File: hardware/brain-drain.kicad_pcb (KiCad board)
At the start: 4 copper layers, 150 x 98 mm, 310 parts, among them J10 SATA 22-pin, J11 SATA 22-pin, J12 SATA 22-pin, J13 SATA 22-pin, J21 KPJX-4S-S, J3 microSD, J4 RJ45 GbE magjack UDE RB1-125B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, J40 Fan GND/5V/TACH/PWM, J41 OLED GND/VCC/SCL/SDA, J5 USB-C rpiboot, J50 M.2 M-key, J6 nRPIBOOT, J7 UART0 GND/TX/RX, M1 CM5002016, Q1 2N7002, Q20 AO4407A, Q31 P-FET -30V 6A DFN3x3, Q32 P-FET -30V 6A DFN3x3, Q33 P-FET -30V 6A DFN3x3, Q34 P-FET -30V 6A DFN3x3, Q41 P-FET -30V 6A DFN3x3, Q42 P-FET -30V 6A DFN3x3, Q43 P-FET -30V 6A DFN3x3, Q44 P-FET -30V 6A DFN3x3, Q51 2N7002, Q52 2N7002, Q53 2N7002, Q54 2N7002, Q61 2N7002, Q62 2N7002, Q63 2N7002, Q64 2N7002, SW1 DIP x8, SW3 door microswitch, U1 USB5744/2G, U10 ASM1153E, U11 ASM1153E, U12 ASM1153E, U13 ASM1153E, U2 USB5744/2G, U20 TPS56637RPAR, U21 TPS56637RPAR, U22 AP63203WU-7, U3 AP2112K-1.2, U50 TPS22965DSGR, U51 AP63203WU-7, U52 TPS22965DSGR, Y1 25MHz CL=20pF, Y10 30MHz CL=16pF, Y11 30MHz CL=16pF, Y12 30MHz CL=16pF, Y13 30MHz CL=16pF, Y2 25MHz CL=20pF

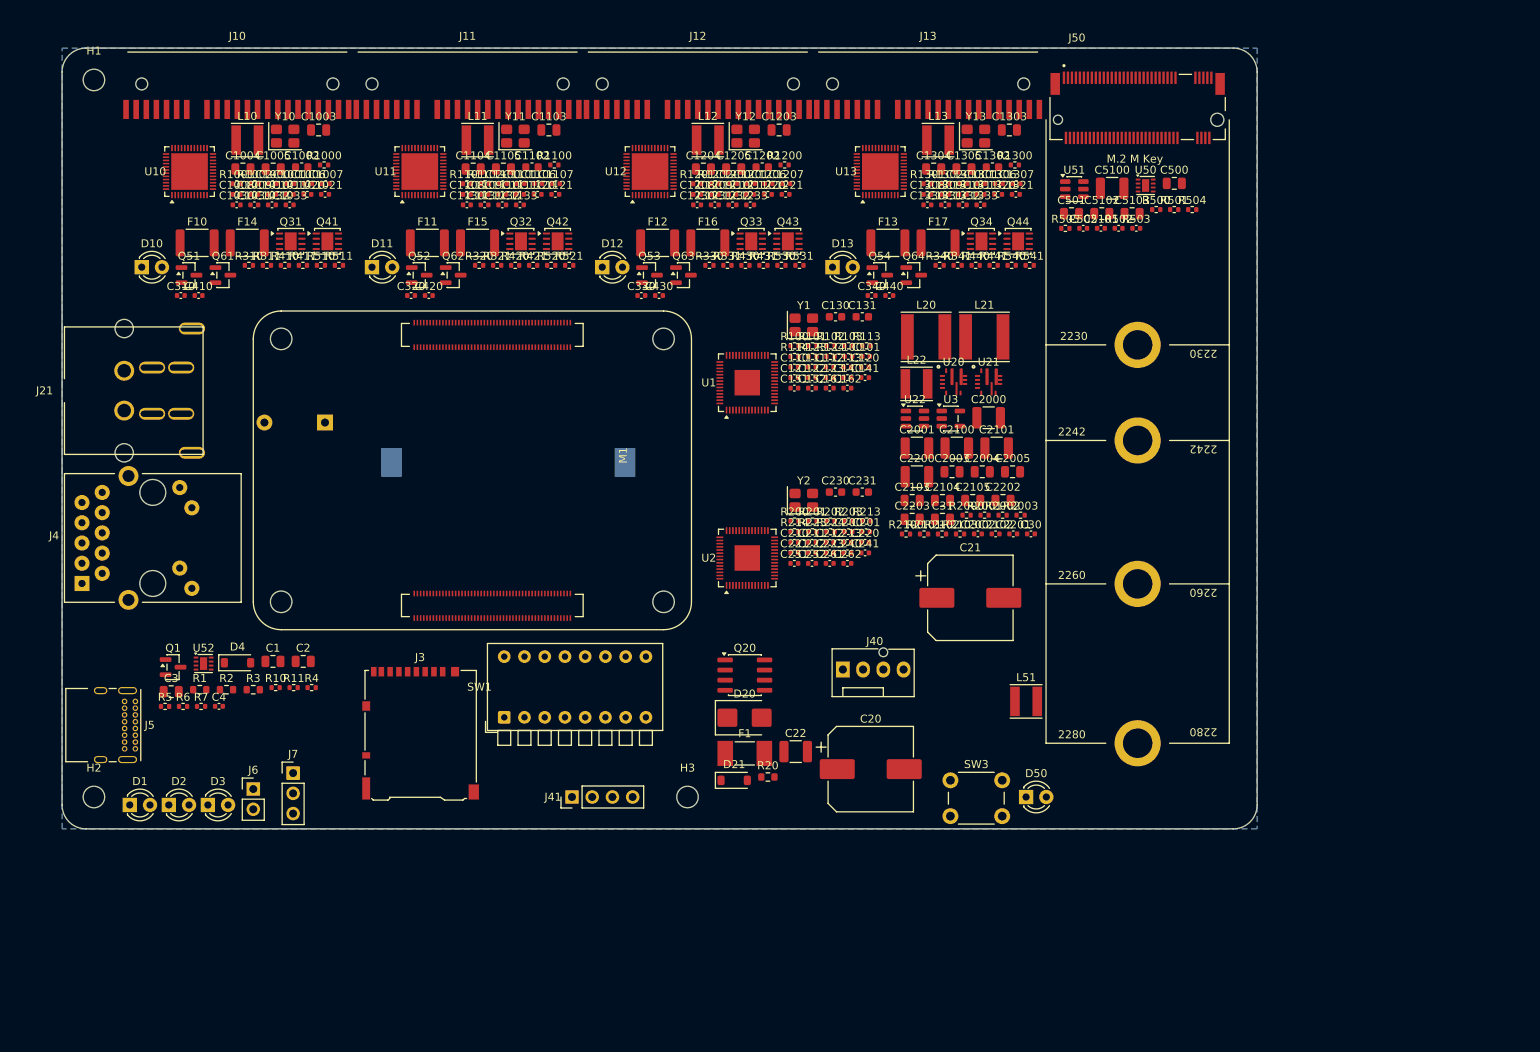
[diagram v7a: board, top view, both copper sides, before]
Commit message: design v2: wireless brain box (C22-C23) — no Ethernet, no buzzer, passive cooler, hinged lid, Wi-Fi AP + QR + phone page, fabrication guide
hardware: 136x100 outline, CM5 wireless antenna edge on the left board edge with a copper-free
strip (rule area), DIN/USB-C/microSD on the right wall, M.2 along the front under the lid, lid
microswitch, CR2032 + service headers on the bottom; magjack and buzzer removed from the
netlist; check_place clean, DRC 0 errors; schematic + connections regenerated, render script
also exports the schematic
software: wifi.py (nmcli / simulated backends, ephemeral key, join, resets), webui.py (stdlib
HTTP phone page: status, certificates, log, join, reset), qr.py, OLED frames with the Wi-Fi QR
code, DIP mode 110 = SERVICE, braindrain wifi-reset; 74 tests, ruff clean; qrcode dependency
enclosure: hinged lid (rear knuckles, filament pin, front snap latch), vents on the antenna side
and front, right-wall cutouts, lid-open scene render
docs: C22/C23, FABRICATION.md (vendors, cost estimate, gates), STATUS R19-R20, panels rear/right,
OLED Wi-Fi mockup, README/ARCHITECTURE/USAGE/BOM/CHANGELOG/HISTORY/tracker updated

Co-Authored-By: Claude Fable 5.1 <noreply@anthropic.com>
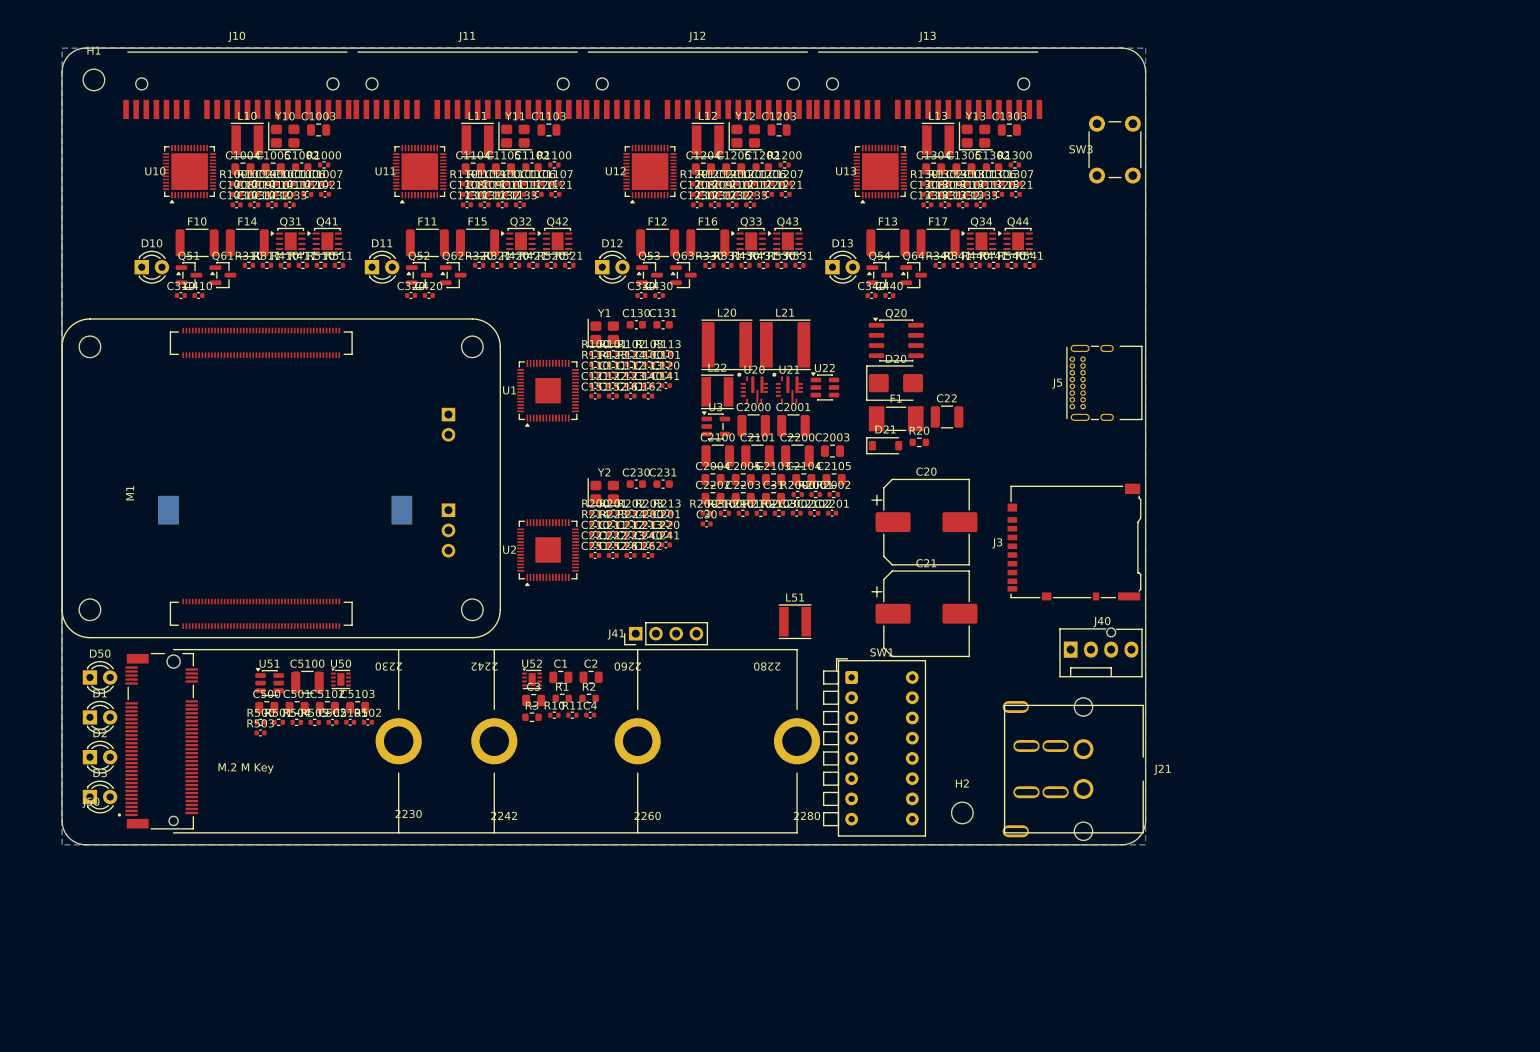
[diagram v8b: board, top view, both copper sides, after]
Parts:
- removed the C340 at (121.6, 51.1)
- removed the C440 at (123.8, 51.1)
- removed the Q64 at (126.9, 48.5)
- removed the R340 at (130.2, 47.3)
- removed the R341 at (132.4, 47.3)
- removed the R440 at (134.7, 47.3)
- removed the R441 at (136.9, 47.3)
- removed the R540 at (139.2, 47.3)
- removed the R541 at (141.4, 47.3)
- BT1: renamed from M1; value CM5002016 -> CR2032; footprint brain-drain:Raspberry-Pi-5-Compute-Module -> Battery:BatteryHolder_Keystone_1060_1x2032; moved to B.Cu
- C1: renamed from R502; value 0R (cap DNP alt) -> 22u 10V; footprint Capacitor_SMD:C_0402_1005Metric -> Capacitor_SMD:C_0805_2012Metric
- C100: renamed from C131; value 4.7u 10V -> 33p; footprint Capacitor_SMD:C_0603_1608Metric -> Capacitor_SMD:C_0402_1005Metric
- C1000: renamed from L10; value 4.7u 1A -> 22p; footprint Inductor_SMD:L_Taiyo-Yuden_NR-40xx -> Capacitor_SMD:C_0402_1005Metric
- C1001: renamed from Y10; value 30MHz CL=16pF -> 22p; footprint Crystal:Crystal_SMD_3225-4Pin_3.2x2.5mm -> Capacitor_SMD:C_0402_1005Metric
- C1002: renamed from C251; value 100n -> 2.2u; footprint Capacitor_SMD:C_0402_1005Metric -> Capacitor_SMD:C_0603_1608Metric
- C1003: renamed from C223; value 100n -> 10u 10V; footprint Capacitor_SMD:C_0402_1005Metric -> Capacitor_SMD:C_0805_2012Metric
- C1004: renamed from C240; value 100n -> 10u 10V; footprint Capacitor_SMD:C_0402_1005Metric -> Capacitor_SMD:C_0805_2012Metric
- C1005: renamed from C241; value 100n -> 10u 10V; footprint Capacitor_SMD:C_0402_1005Metric -> Capacitor_SMD:C_0805_2012Metric
- C1006: renamed from C1003; value 10u 10V -> 100n; footprint Capacitor_SMD:C_0805_2012Metric -> Capacitor_SMD:C_0402_1005Metric
- C1007: renamed from C1004; value 10u 10V -> 100n; footprint Capacitor_SMD:C_0805_2012Metric -> Capacitor_SMD:C_0402_1005Metric
- C1008: renamed from C1005; value 10u 10V -> 100n; footprint Capacitor_SMD:C_0805_2012Metric -> Capacitor_SMD:C_0402_1005Metric
- C1009: renamed from C1002; value 2.2u -> 100n; footprint Capacitor_SMD:C_0603_1608Metric -> Capacitor_SMD:C_0402_1005Metric
- C101: renamed from R100; value 12.0k 1% -> 33p; footprint Resistor_SMD:R_0402_1005Metric -> Capacitor_SMD:C_0402_1005Metric
- C1010: renamed from R1000; value 12.1k 1% -> 100n; footprint Resistor_SMD:R_0402_1005Metric -> Capacitor_SMD:C_0402_1005Metric
- C1011: renamed from R1001; value 10k -> 100n; footprint Resistor_SMD:R_0402_1005Metric -> Capacitor_SMD:C_0402_1005Metric
- C1020: renamed from R1002; value 470 -> 100n; footprint Resistor_SMD:R_0402_1005Metric -> Capacitor_SMD:C_0402_1005Metric
- C1021: renamed from C1000; value 22p -> 100n
- C1030: renamed from C1001; value 22p -> 10n
- C1031: renamed from C1006; value 100n -> 10n
- C1032: renamed from C1007; value 100n -> 10n
- C1033: renamed from C1008; value 100n -> 10n
- C110: renamed from R101; value 10k -> 100n; footprint Resistor_SMD:R_0402_1005Metric -> Capacitor_SMD:C_0402_1005Metric
- C1100: renamed from L11; value 4.7u 1A -> 22p; footprint Inductor_SMD:L_Taiyo-Yuden_NR-40xx -> Capacitor_SMD:C_0402_1005Metric
- C1101: renamed from Y11; value 30MHz CL=16pF -> 22p; footprint Crystal:Crystal_SMD_3225-4Pin_3.2x2.5mm -> Capacitor_SMD:C_0402_1005Metric
- C1102: renamed from R510; value 10k -> 2.2u; footprint Resistor_SMD:R_0402_1005Metric -> Capacitor_SMD:C_0603_1608Metric
- C1103: renamed from R311; value 10k -> 10u 10V; footprint Resistor_SMD:R_0402_1005Metric -> Capacitor_SMD:C_0805_2012Metric
- C1104: renamed from R410; value 100k -> 10u 10V; footprint Resistor_SMD:R_0402_1005Metric -> Capacitor_SMD:C_0805_2012Metric
- C1105: renamed from R411; value 10k -> 10u 10V; footprint Resistor_SMD:R_0402_1005Metric -> Capacitor_SMD:C_0805_2012Metric
- C1106: renamed from C1103; value 10u 10V -> 100n; footprint Capacitor_SMD:C_0805_2012Metric -> Capacitor_SMD:C_0402_1005Metric
- C1107: renamed from C1104; value 10u 10V -> 100n; footprint Capacitor_SMD:C_0805_2012Metric -> Capacitor_SMD:C_0402_1005Metric
- C1108: renamed from C1105; value 10u 10V -> 100n; footprint Capacitor_SMD:C_0805_2012Metric -> Capacitor_SMD:C_0402_1005Metric
- C1109: renamed from C1102; value 2.2u -> 100n; footprint Capacitor_SMD:C_0603_1608Metric -> Capacitor_SMD:C_0402_1005Metric
- C111: renamed from R102; value 10k -> 100n; footprint Resistor_SMD:R_0402_1005Metric -> Capacitor_SMD:C_0402_1005Metric
- C1110: renamed from R1100; value 12.1k 1% -> 100n; footprint Resistor_SMD:R_0402_1005Metric -> Capacitor_SMD:C_0402_1005Metric
- C1111: renamed from R1101; value 10k -> 100n; footprint Resistor_SMD:R_0402_1005Metric -> Capacitor_SMD:C_0402_1005Metric
- C112: renamed from R103; value 200k -> 100n; footprint Resistor_SMD:R_0402_1005Metric -> Capacitor_SMD:C_0402_1005Metric
- C1120: renamed from R1102; value 470 -> 100n; footprint Resistor_SMD:R_0402_1005Metric -> Capacitor_SMD:C_0402_1005Metric
- C1121: renamed from C1100; value 22p -> 100n
- C113: renamed from R113; value 10k -> 100n; footprint Resistor_SMD:R_0402_1005Metric -> Capacitor_SMD:C_0402_1005Metric
- C1130: renamed from C1101; value 22p -> 10n
- C1131: renamed from C1106; value 100n -> 10n
- C1132: renamed from C1107; value 100n -> 10n
- C1133: renamed from C1108; value 100n -> 10n
- C120: renamed from R114; value 10k -> 100n; footprint Resistor_SMD:R_0402_1005Metric -> Capacitor_SMD:C_0402_1005Metric
- C1200: renamed from L12; value 4.7u 1A -> 22p; footprint Inductor_SMD:L_Taiyo-Yuden_NR-40xx -> Capacitor_SMD:C_0402_1005Metric
- C1201: renamed from Y12; value 30MHz CL=16pF -> 22p; footprint Crystal:Crystal_SMD_3225-4Pin_3.2x2.5mm -> Capacitor_SMD:C_0402_1005Metric
- C1202: renamed from R520; value 10k -> 2.2u; footprint Resistor_SMD:R_0402_1005Metric -> Capacitor_SMD:C_0603_1608Metric
- C1203: renamed from R321; value 10k -> 10u 10V; footprint Resistor_SMD:R_0402_1005Metric -> Capacitor_SMD:C_0805_2012Metric
- C1204: renamed from R420; value 100k -> 10u 10V; footprint Resistor_SMD:R_0402_1005Metric -> Capacitor_SMD:C_0805_2012Metric
- C1205: renamed from R421; value 10k -> 10u 10V; footprint Resistor_SMD:R_0402_1005Metric -> Capacitor_SMD:C_0805_2012Metric
- C1206: renamed from C1203; value 10u 10V -> 100n; footprint Capacitor_SMD:C_0805_2012Metric -> Capacitor_SMD:C_0402_1005Metric
- C1207: renamed from C1204; value 10u 10V -> 100n; footprint Capacitor_SMD:C_0805_2012Metric -> Capacitor_SMD:C_0402_1005Metric
- C1208: renamed from C1205; value 10u 10V -> 100n; footprint Capacitor_SMD:C_0805_2012Metric -> Capacitor_SMD:C_0402_1005Metric
- C1209: renamed from C1202; value 2.2u -> 100n; footprint Capacitor_SMD:C_0603_1608Metric -> Capacitor_SMD:C_0402_1005Metric
- C121: renamed from R123; value 10k -> 100n; footprint Resistor_SMD:R_0402_1005Metric -> Capacitor_SMD:C_0402_1005Metric
- C1210: renamed from R1200; value 12.1k 1% -> 100n; footprint Resistor_SMD:R_0402_1005Metric -> Capacitor_SMD:C_0402_1005Metric
- C1211: renamed from R1201; value 10k -> 100n; footprint Resistor_SMD:R_0402_1005Metric -> Capacitor_SMD:C_0402_1005Metric
- C122: renamed from R124; value 10k -> 100n; footprint Resistor_SMD:R_0402_1005Metric -> Capacitor_SMD:C_0402_1005Metric
- C1220: renamed from R1202; value 470 -> 100n; footprint Resistor_SMD:R_0402_1005Metric -> Capacitor_SMD:C_0402_1005Metric
- C1221: renamed from C1200; value 22p -> 100n
- C123: renamed from C100; value 33p -> 100n
- C1230: renamed from C1201; value 22p -> 10n
- C1231: renamed from C1206; value 100n -> 10n
- C1232: renamed from C1207; value 100n -> 10n
- C1233: renamed from C1208; value 100n -> 10n
- C130: renamed from R3; value 1k -> 4.7u 10V; footprint Resistor_SMD:R_0603_1608Metric -> Capacitor_SMD:C_0603_1608Metric
- C1300: renamed from L13; value 4.7u 1A -> 22p; footprint Inductor_SMD:L_Taiyo-Yuden_NR-40xx -> Capacitor_SMD:C_0402_1005Metric
- C1301: renamed from Y13; value 30MHz CL=16pF -> 22p; footprint Crystal:Crystal_SMD_3225-4Pin_3.2x2.5mm -> Capacitor_SMD:C_0402_1005Metric
- C1302: renamed from R530; value 10k -> 2.2u; footprint Resistor_SMD:R_0402_1005Metric -> Capacitor_SMD:C_0603_1608Metric
- C1303: renamed from R331; value 10k -> 10u 10V; footprint Resistor_SMD:R_0402_1005Metric -> Capacitor_SMD:C_0805_2012Metric
- C1304: renamed from R430; value 100k -> 10u 10V; footprint Resistor_SMD:R_0402_1005Metric -> Capacitor_SMD:C_0805_2012Metric
- C1305: renamed from R431; value 10k -> 10u 10V; footprint Resistor_SMD:R_0402_1005Metric -> Capacitor_SMD:C_0805_2012Metric
- C1306: renamed from C1303; value 10u 10V -> 100n; footprint Capacitor_SMD:C_0805_2012Metric -> Capacitor_SMD:C_0402_1005Metric
- C1307: renamed from C1304; value 10u 10V -> 100n; footprint Capacitor_SMD:C_0805_2012Metric -> Capacitor_SMD:C_0402_1005Metric
- C1308: renamed from C1305; value 10u 10V -> 100n; footprint Capacitor_SMD:C_0805_2012Metric -> Capacitor_SMD:C_0402_1005Metric
- C1309: renamed from C1302; value 2.2u -> 100n; footprint Capacitor_SMD:C_0603_1608Metric -> Capacitor_SMD:C_0402_1005Metric
- C131: renamed from R10; value 10k -> 4.7u 10V; footprint Resistor_SMD:R_0402_1005Metric -> Capacitor_SMD:C_0603_1608Metric
- C1310: renamed from R1300; value 12.1k 1% -> 100n; footprint Resistor_SMD:R_0402_1005Metric -> Capacitor_SMD:C_0402_1005Metric
- C1311: renamed from R1301; value 10k -> 100n; footprint Resistor_SMD:R_0402_1005Metric -> Capacitor_SMD:C_0402_1005Metric
- C1320: renamed from R1302; value 470 -> 100n; footprint Resistor_SMD:R_0402_1005Metric -> Capacitor_SMD:C_0402_1005Metric
- C1321: renamed from C1300; value 22p -> 100n
- C1330: renamed from C1301; value 22p -> 10n
- C1331: renamed from C1306; value 100n -> 10n
- C1332: renamed from C1307; value 100n -> 10n
- C1333: renamed from C1308; value 100n -> 10n
- C140: renamed from C101; value 33p -> 100n
- C2: renamed from R503; value 0R (cap DNP alt) -> 22u 10V; footprint Capacitor_SMD:C_0402_1005Metric -> Capacitor_SMD:C_0805_2012Metric
- C20: renamed from J21; value KPJX-4S-S -> 680u 25V low-ESR; footprint brain-drain:Kycon_KPJX-4S-S -> Capacitor_SMD:CP_Elec_10x10.5
- C200: renamed from C231; value 4.7u 10V -> 33p; footprint Capacitor_SMD:C_0603_1608Metric -> Capacitor_SMD:C_0402_1005Metric
- C2000: renamed from U21; value TPS56637RPAR -> 10u 25V; footprint brain-drain:Texas_RPA0010A_VQFN-HR-10_3x3mm -> Capacitor_SMD:C_1210_3225Metric
- C2001: renamed from U22; value AP63203WU-7 -> 10u 25V; footprint Package_TO_SOT_SMD:TSOT-23-6 -> Capacitor_SMD:C_1210_3225Metric
- C2002: renamed from R2101; value 10k -> 100n 25V; footprint Resistor_SMD:R_0402_1005Metric -> Capacitor_SMD:C_0402_1005Metric
- C2003: renamed from C2100; value 10u 25V -> 22u 10V; footprint Capacitor_SMD:C_1210_3225Metric -> Capacitor_SMD:C_0805_2012Metric
- C2004: renamed from C2101; value 10u 25V -> 22u 10V; footprint Capacitor_SMD:C_1210_3225Metric -> Capacitor_SMD:C_0805_2012Metric
- C2005: renamed from C2200; value 10u 25V -> 22u 10V; footprint Capacitor_SMD:C_1210_3225Metric -> Capacitor_SMD:C_0805_2012Metric
- C201: renamed from R200; value 12.0k 1% -> 33p; footprint Resistor_SMD:R_0402_1005Metric -> Capacitor_SMD:C_0402_1005Metric
- C210: renamed from R201; value 10k -> 100n; footprint Resistor_SMD:R_0402_1005Metric -> Capacitor_SMD:C_0402_1005Metric
- C2100: renamed from U3; value AP2112K-1.2 -> 10u 25V; footprint Package_TO_SOT_SMD:SOT-23-5 -> Capacitor_SMD:C_1210_3225Metric
- C2102: renamed from R2102; value 100k -> 100n 25V; footprint Resistor_SMD:R_0402_1005Metric -> Capacitor_SMD:C_0402_1005Metric
- C211: renamed from R202; value 10k -> 100n; footprint Resistor_SMD:R_0402_1005Metric -> Capacitor_SMD:C_0402_1005Metric
- C212: renamed from R203; value 200k -> 100n; footprint Resistor_SMD:R_0402_1005Metric -> Capacitor_SMD:C_0402_1005Metric
- C213: renamed from R213; value 10k -> 100n; footprint Resistor_SMD:R_0402_1005Metric -> Capacitor_SMD:C_0402_1005Metric
- C22: renamed from Q20; value AO4407A -> 10u 25V; footprint Package_SO:SOIC-8_3.9x4.9mm_P1.27mm -> Capacitor_SMD:C_1210_3225Metric
- C220: renamed from R214; value 10k -> 100n; footprint Resistor_SMD:R_0402_1005Metric -> Capacitor_SMD:C_0402_1005Metric
- C2201: renamed from R2103; value 10k -> 100n 10V; footprint Resistor_SMD:R_0402_1005Metric -> Capacitor_SMD:C_0402_1005Metric
- C221: renamed from R223; value 10k -> 100n; footprint Resistor_SMD:R_0402_1005Metric -> Capacitor_SMD:C_0402_1005Metric
- C222: renamed from R224; value 10k -> 100n; footprint Resistor_SMD:R_0402_1005Metric -> Capacitor_SMD:C_0402_1005Metric
- C223: renamed from C200; value 33p -> 100n
- C230: renamed from C122; value 100n -> 4.7u 10V; footprint Capacitor_SMD:C_0402_1005Metric -> Capacitor_SMD:C_0603_1608Metric
- C231: renamed from C123; value 100n -> 4.7u 10V; footprint Capacitor_SMD:C_0402_1005Metric -> Capacitor_SMD:C_0603_1608Metric
- C240: renamed from C201; value 33p -> 100n
- C3: renamed from Q1; value 2N7002 -> 10u 10V; footprint Package_TO_SOT_SMD:SOT-23 -> Capacitor_SMD:C_0805_2012Metric
- C30: renamed from C2002; value 100n 25V -> 1u 10V
- C31: renamed from C2105; value 22u 10V -> 10u 10V
- C310: renamed from Q41; value P-FET -30V 6A DFN3x3 -> 100n; footprint Package_DFN_QFN:DFN-8-1EP_3x3mm_P0.65mm_EP1.5x2.25mm -> Capacitor_SMD:C_0402_1005Metric
- C320: renamed from Q42; value P-FET -30V 6A DFN3x3 -> 100n; footprint Package_DFN_QFN:DFN-8-1EP_3x3mm_P0.65mm_EP1.5x2.25mm -> Capacitor_SMD:C_0402_1005Metric
- C330: renamed from Q43; value P-FET -30V 6A DFN3x3 -> 100n; footprint Package_DFN_QFN:DFN-8-1EP_3x3mm_P0.65mm_EP1.5x2.25mm -> Capacitor_SMD:C_0402_1005Metric
- C340: renamed from Q44; value P-FET -30V 6A DFN3x3 -> 100n; footprint Package_DFN_QFN:DFN-8-1EP_3x3mm_P0.65mm_EP1.5x2.25mm -> Capacitor_SMD:C_0402_1005Metric
- C4: renamed from R1; value 1k -> 1u 10V; footprint Resistor_SMD:R_0603_1608Metric -> Capacitor_SMD:C_0402_1005Metric
- C410: renamed from Q51; value 2N7002 -> 100n; footprint Package_TO_SOT_SMD:SOT-23 -> Capacitor_SMD:C_0402_1005Metric
- C420: renamed from Q52; value 2N7002 -> 100n; footprint Package_TO_SOT_SMD:SOT-23 -> Capacitor_SMD:C_0402_1005Metric
- C430: renamed from Q53; value 2N7002 -> 100n; footprint Package_TO_SOT_SMD:SOT-23 -> Capacitor_SMD:C_0402_1005Metric
- C440: renamed from Q54; value 2N7002 -> 100n; footprint Package_TO_SOT_SMD:SOT-23 -> Capacitor_SMD:C_0402_1005Metric
- C500: renamed from U51; value AP63203WU-7 -> 10u 10V; footprint Package_TO_SOT_SMD:TSOT-23-6 -> Capacitor_SMD:C_0805_2012Metric
- C501: renamed from C5100; value 10u 25V -> 22u 10V; footprint Capacitor_SMD:C_1210_3225Metric -> Capacitor_SMD:C_0805_2012Metric
- C502: renamed from R501; value 10k -> 1n; footprint Resistor_SMD:R_0402_1005Metric -> Capacitor_SMD:C_0402_1005Metric
- C5100: renamed from C2201; value 100n 10V -> 10u 25V; footprint Capacitor_SMD:C_0402_1005Metric -> Capacitor_SMD:C_1210_3225Metric
- C5101: renamed from R504; value 10k -> 100n 10V; footprint Resistor_SMD:R_0402_1005Metric -> Capacitor_SMD:C_0402_1005Metric
- C5102: renamed from U50; value TPS22965DSGR -> 22u 10V; footprint Package_SON:Texas_DSG0008A_WSON-8-1EP_2x2mm_P0.5mm_EP0.9x1.6mm -> Capacitor_SMD:C_0805_2012Metric
- C5103: renamed from C500; value 10u 10V -> 22u 10V
- D1: renamed from J40; value Fan GND/5V/TACH/PWM -> green PWR; footprint Connector:FanPinHeader_1x04_P2.54mm_Vertical -> LED_THT:LED_D3.0mm
- D10: renamed from U2; value USB5744/2G -> blue bay activity; footprint Package_DFN_QFN:QFN-56-1EP_7x7mm_P0.4mm_EP3.2x3.2mm -> LED_THT:LED_D3.0mm
- D2: renamed from D1; value green PWR -> green ACT
- D20: renamed from D50; value blue M.2 activity -> SMBJ15A; footprint LED_THT:LED_D3.0mm -> Diode_SMD:D_SMB
- D21: renamed from D20; value SMBJ15A -> 12V 0.5W; footprint Diode_SMD:D_SMB -> Diode_SMD:D_SOD-123
- D3: renamed from D2; value green ACT -> red STATUS
- D50: renamed from J13; value SATA 22-pin -> blue M.2 activity; footprint brain-drain:SATA_22pin_Receptacle_RA -> LED_THT:LED_D3.0mm
- F1: renamed from SW3; value door microswitch -> 10A slow 0453010.MR; footprint Button_Switch_THT:SW_PUSH_6mm -> Fuse:Fuse_Littelfuse-NANO2-451_453
- F10: renamed from C1009; value 100n -> 3A hold 1812; footprint Capacitor_SMD:C_0402_1005Metric -> Fuse:Fuse_1812_4532Metric
- F11: renamed from C1109; value 100n -> 3A hold 1812; footprint Capacitor_SMD:C_0402_1005Metric -> Fuse:Fuse_1812_4532Metric
- F12: renamed from C1209; value 100n -> 3A hold 1812; footprint Capacitor_SMD:C_0402_1005Metric -> Fuse:Fuse_1812_4532Metric
- F13: renamed from C1309; value 100n -> 3A hold 1812; footprint Capacitor_SMD:C_0402_1005Metric -> Fuse:Fuse_1812_4532Metric
- F14: renamed from C1010; value 100n -> 2A hold 1812; footprint Capacitor_SMD:C_0402_1005Metric -> Fuse:Fuse_1812_4532Metric
- F15: renamed from C1110; value 100n -> 2A hold 1812; footprint Capacitor_SMD:C_0402_1005Metric -> Fuse:Fuse_1812_4532Metric
- F16: renamed from C1210; value 100n -> 2A hold 1812; footprint Capacitor_SMD:C_0402_1005Metric -> Fuse:Fuse_1812_4532Metric
- F17: renamed from C1310; value 100n -> 2A hold 1812; footprint Capacitor_SMD:C_0402_1005Metric -> Fuse:Fuse_1812_4532Metric
- J10: renamed from U1; value USB5744/2G -> SATA 22-pin; footprint Package_DFN_QFN:QFN-56-1EP_7x7mm_P0.4mm_EP3.2x3.2mm -> brain-drain:SATA_22pin_Receptacle_RA
- J21: renamed from H3; value M2.5 -> KPJX-4S-S; footprint MountingHole:MountingHole_2.7mm_M2.5 -> brain-drain:Kycon_KPJX-4S-S
- J3: renamed from BZ1; value 5V magnetic -> microSD; footprint Buzzer_Beeper:Buzzer_12x9.5RM7.6 -> Connector_Card:microSD_HC_Hirose_DM3AT-SF-PEJM5; moved to F.Cu
- J40: renamed from J7; value UART0 GND/TX/RX -> Fan GND/5V/TACH/PWM; footprint Connector_PinHeader_2.54mm:PinHeader_1x03_P2.54mm_Vertical -> Connector:FanPinHeader_1x04_P2.54mm_Vertical
- J41: renamed from SW1; value DIP x8 -> OLED GND/VCC/SCL/SDA; footprint Button_Switch_THT:SW_DIP_SPSTx08_Piano_10.8x21.88mm_W7.62mm_P2.54mm -> Connector_PinHeader_2.54mm:PinHeader_1x04_P2.54mm_Vertical
- J5: renamed from J41; value OLED GND/VCC/SCL/SDA -> USB-C rpiboot; footprint Connector_PinHeader_2.54mm:PinHeader_1x04_P2.54mm_Vertical -> Connector_USB:USB_C_Receptacle_GCT_USB4085
- J50: renamed from U13; value ASM1153E -> M.2 M-key; footprint Package_DFN_QFN:QFN-48-1EP_6x6mm_P0.4mm_EP4.6x4.6mm -> brain-drain:M2_Socket3_MKey_CM5IO
- J6: renamed from BT1; value CR2032 -> nRPIBOOT; footprint Battery:BatteryHolder_Keystone_1060_1x2032 -> Connector_PinHeader_2.54mm:PinHeader_1x02_P2.54mm_Vertical
- J7: renamed from J6; value nRPIBOOT -> UART0 GND/TX/RX; footprint Connector_PinHeader_2.54mm:PinHeader_1x02_P2.54mm_Vertical -> Connector_PinHeader_2.54mm:PinHeader_1x03_P2.54mm_Vertical; moved to B.Cu
- L10: renamed from C221; value 100n -> 4.7u 1A; footprint Capacitor_SMD:C_0402_1005Metric -> Inductor_SMD:L_Taiyo-Yuden_NR-40xx
- L11: renamed from Q61; value 2N7002 -> 4.7u 1A; footprint Package_TO_SOT_SMD:SOT-23 -> Inductor_SMD:L_Taiyo-Yuden_NR-40xx
- L12: renamed from Q62; value 2N7002 -> 4.7u 1A; footprint Package_TO_SOT_SMD:SOT-23 -> Inductor_SMD:L_Taiyo-Yuden_NR-40xx
- L13: renamed from Q63; value 2N7002 -> 4.7u 1A; footprint Package_TO_SOT_SMD:SOT-23 -> Inductor_SMD:L_Taiyo-Yuden_NR-40xx
- L20: renamed from C22; value 10u 25V -> 2.2u 8A; footprint Capacitor_SMD:C_1210_3225Metric -> Inductor_SMD:L_Taiyo-Yuden_NR-60xx
- L21: renamed from D21; value 12V 0.5W -> 2.2u 8A; footprint Diode_SMD:D_SOD-123 -> Inductor_SMD:L_Taiyo-Yuden_NR-60xx
- L22: renamed from R20; value 100k -> 4.7u 3A; footprint Resistor_SMD:R_0603_1608Metric -> Inductor_SMD:L_Taiyo-Yuden_NR-40xx
- L51: renamed from C21; value 680u 25V low-ESR -> 4.7u 3A; footprint Capacitor_SMD:CP_Elec_10x10.5 -> Inductor_SMD:L_Taiyo-Yuden_NR-40xx
- M1: renamed from L51; value 4.7u 3A -> CM5002016; footprint Inductor_SMD:L_Taiyo-Yuden_NR-40xx -> brain-drain:Raspberry-Pi-5-Compute-Module
- Q20: renamed from J50; value M.2 M-key -> AO4407A; footprint brain-drain:M2_Socket3_MKey_CM5IO -> Package_SO:SOIC-8_3.9x4.9mm_P1.27mm
- Q31: renamed from C1011; value 100n -> P-FET -30V 6A DFN3x3; footprint Capacitor_SMD:C_0402_1005Metric -> Package_DFN_QFN:DFN-8-1EP_3x3mm_P0.65mm_EP1.5x2.25mm
- Q32: renamed from C1111; value 100n -> P-FET -30V 6A DFN3x3; footprint Capacitor_SMD:C_0402_1005Metric -> Package_DFN_QFN:DFN-8-1EP_3x3mm_P0.65mm_EP1.5x2.25mm
- Q33: renamed from C1211; value 100n -> P-FET -30V 6A DFN3x3; footprint Capacitor_SMD:C_0402_1005Metric -> Package_DFN_QFN:DFN-8-1EP_3x3mm_P0.65mm_EP1.5x2.25mm
- Q34: renamed from C1311; value 100n -> P-FET -30V 6A DFN3x3; footprint Capacitor_SMD:C_0402_1005Metric -> Package_DFN_QFN:DFN-8-1EP_3x3mm_P0.65mm_EP1.5x2.25mm
- Q41: renamed from C1020; value 100n -> P-FET -30V 6A DFN3x3; footprint Capacitor_SMD:C_0402_1005Metric -> Package_DFN_QFN:DFN-8-1EP_3x3mm_P0.65mm_EP1.5x2.25mm
- Q42: renamed from C1120; value 100n -> P-FET -30V 6A DFN3x3; footprint Capacitor_SMD:C_0402_1005Metric -> Package_DFN_QFN:DFN-8-1EP_3x3mm_P0.65mm_EP1.5x2.25mm
- Q43: renamed from C1220; value 100n -> P-FET -30V 6A DFN3x3; footprint Capacitor_SMD:C_0402_1005Metric -> Package_DFN_QFN:DFN-8-1EP_3x3mm_P0.65mm_EP1.5x2.25mm
- Q44: renamed from C1320; value 100n -> P-FET -30V 6A DFN3x3; footprint Capacitor_SMD:C_0402_1005Metric -> Package_DFN_QFN:DFN-8-1EP_3x3mm_P0.65mm_EP1.5x2.25mm
- Q51: renamed from C1021; value 100n -> 2N7002; footprint Capacitor_SMD:C_0402_1005Metric -> Package_TO_SOT_SMD:SOT-23
- Q52: renamed from C1121; value 100n -> 2N7002; footprint Capacitor_SMD:C_0402_1005Metric -> Package_TO_SOT_SMD:SOT-23
- Q53: renamed from C1221; value 100n -> 2N7002; footprint Capacitor_SMD:C_0402_1005Metric -> Package_TO_SOT_SMD:SOT-23
- Q54: renamed from C1321; value 100n -> 2N7002; footprint Capacitor_SMD:C_0402_1005Metric -> Package_TO_SOT_SMD:SOT-23
- Q61: renamed from C1030; value 10n -> 2N7002; footprint Capacitor_SMD:C_0402_1005Metric -> Package_TO_SOT_SMD:SOT-23
- Q62: renamed from C1130; value 10n -> 2N7002; footprint Capacitor_SMD:C_0402_1005Metric -> Package_TO_SOT_SMD:SOT-23
- Q63: renamed from C1230; value 10n -> 2N7002; footprint Capacitor_SMD:C_0402_1005Metric -> Package_TO_SOT_SMD:SOT-23
- Q64: renamed from C1330; value 10n -> 2N7002; footprint Capacitor_SMD:C_0402_1005Metric -> Package_TO_SOT_SMD:SOT-23
- R1: renamed from U52; value TPS22965DSGR -> 1k; footprint Package_SON:Texas_DSG0008A_WSON-8-1EP_2x2mm_P0.5mm_EP0.9x1.6mm -> Resistor_SMD:R_0603_1608Metric
- R10: renamed from C2; value 22u 10V -> 10k; footprint Capacitor_SMD:C_0805_2012Metric -> Resistor_SMD:R_0402_1005Metric
- R100: renamed from R11; value 10k -> 12.0k 1%
- R1000: renamed from C252; value 100n -> 12.1k 1%; footprint Capacitor_SMD:C_0402_1005Metric -> Resistor_SMD:R_0402_1005Metric
- R1001: renamed from C261; value 100n -> 10k; footprint Capacitor_SMD:C_0402_1005Metric -> Resistor_SMD:R_0402_1005Metric
- R1002: renamed from C262; value 100n -> 470; footprint Capacitor_SMD:C_0402_1005Metric -> Resistor_SMD:R_0402_1005Metric
- R101: renamed from R4; value 1k -> 10k
- R102: renamed from R5; value 100k -> 10k
- R103: renamed from R6; value 470 -> 200k
- R11: renamed from C3; value 10u 10V -> 10k; footprint Capacitor_SMD:C_0805_2012Metric -> Resistor_SMD:R_0402_1005Metric
- R1100: renamed from R511; value 1k -> 12.1k 1%
- R1101: renamed from C310; value 100n -> 10k; footprint Capacitor_SMD:C_0402_1005Metric -> Resistor_SMD:R_0402_1005Metric
- R1102: renamed from C410; value 100n -> 470; footprint Capacitor_SMD:C_0402_1005Metric -> Resistor_SMD:R_0402_1005Metric
- R113: renamed from R7; value 470 -> 10k
- R114: renamed from C4; value 1u 10V -> 10k; footprint Capacitor_SMD:C_0402_1005Metric -> Resistor_SMD:R_0402_1005Metric
- R1200: renamed from R521; value 1k -> 12.1k 1%
- R1201: renamed from C320; value 100n -> 10k; footprint Capacitor_SMD:C_0402_1005Metric -> Resistor_SMD:R_0402_1005Metric
- R1202: renamed from C420; value 100n -> 470; footprint Capacitor_SMD:C_0402_1005Metric -> Resistor_SMD:R_0402_1005Metric
- R123: renamed from Y1; value 25MHz CL=20pF -> 10k; footprint Crystal:Crystal_SMD_3225-4Pin_3.2x2.5mm -> Resistor_SMD:R_0402_1005Metric
- R124: renamed from C130; value 4.7u 10V -> 10k; footprint Capacitor_SMD:C_0603_1608Metric -> Resistor_SMD:R_0402_1005Metric
- R1300: renamed from R531; value 1k -> 12.1k 1%
- R1301: renamed from C330; value 100n -> 10k; footprint Capacitor_SMD:C_0402_1005Metric -> Resistor_SMD:R_0402_1005Metric
- R1302: renamed from C430; value 100n -> 470; footprint Capacitor_SMD:C_0402_1005Metric -> Resistor_SMD:R_0402_1005Metric
- R2: renamed from D4; value 1N4148W -> 1k; footprint Diode_SMD:D_SOD-123 -> Resistor_SMD:R_0603_1608Metric
- R20: renamed from F1; value 10A slow 0453010.MR -> 100k; footprint Fuse:Fuse_Littelfuse-NANO2-451_453 -> Resistor_SMD:R_0603_1608Metric
- R200: renamed from C140; value 100n -> 12.0k 1%; footprint Capacitor_SMD:C_0402_1005Metric -> Resistor_SMD:R_0402_1005Metric
- R2000: renamed from C2202; value 22u 10V -> 73.2k; footprint Capacitor_SMD:C_0805_2012Metric -> Resistor_SMD:R_0402_1005Metric
- R2001: renamed from C2203; value 22u 10V -> 10k; footprint Capacitor_SMD:C_0805_2012Metric -> Resistor_SMD:R_0402_1005Metric
- R2002: renamed from C31; value 10u 10V -> 100k; footprint Capacitor_SMD:C_0805_2012Metric -> Resistor_SMD:R_0402_1005Metric
- R2003: renamed from R2000; value 73.2k -> 10k
- R201: renamed from C141; value 100n -> 10k; footprint Capacitor_SMD:C_0402_1005Metric -> Resistor_SMD:R_0402_1005Metric
- R202: renamed from C151; value 100n -> 10k; footprint Capacitor_SMD:C_0402_1005Metric -> Resistor_SMD:R_0402_1005Metric
- R203: renamed from C152; value 100n -> 200k; footprint Capacitor_SMD:C_0402_1005Metric -> Resistor_SMD:R_0402_1005Metric
- R2100: renamed from R2001; value 10k -> 73.2k
- R2101: renamed from R2002; value 100k -> 10k
- R2102: renamed from R2003; value 10k -> 100k
- R2103: renamed from R2100; value 73.2k -> 10k
- R213: renamed from C161; value 100n -> 10k; footprint Capacitor_SMD:C_0402_1005Metric -> Resistor_SMD:R_0402_1005Metric
- R214: renamed from C162; value 100n -> 10k; footprint Capacitor_SMD:C_0402_1005Metric -> Resistor_SMD:R_0402_1005Metric
- R223: renamed from Y2; value 25MHz CL=20pF -> 10k; footprint Crystal:Crystal_SMD_3225-4Pin_3.2x2.5mm -> Resistor_SMD:R_0402_1005Metric
- R224: renamed from C230; value 4.7u 10V -> 10k; footprint Capacitor_SMD:C_0603_1608Metric -> Resistor_SMD:R_0402_1005Metric
- R3: renamed from C1; value 22u 10V -> 1k; footprint Capacitor_SMD:C_0805_2012Metric -> Resistor_SMD:R_0603_1608Metric
- R310: renamed from C1031; value 10n -> 100k; footprint Capacitor_SMD:C_0402_1005Metric -> Resistor_SMD:R_0402_1005Metric
- R311: renamed from C1032; value 10n -> 10k; footprint Capacitor_SMD:C_0402_1005Metric -> Resistor_SMD:R_0402_1005Metric
- R320: renamed from C1131; value 10n -> 100k; footprint Capacitor_SMD:C_0402_1005Metric -> Resistor_SMD:R_0402_1005Metric
- R321: renamed from C1132; value 10n -> 10k; footprint Capacitor_SMD:C_0402_1005Metric -> Resistor_SMD:R_0402_1005Metric
- R330: renamed from C1231; value 10n -> 100k; footprint Capacitor_SMD:C_0402_1005Metric -> Resistor_SMD:R_0402_1005Metric
- R331: renamed from C1232; value 10n -> 10k; footprint Capacitor_SMD:C_0402_1005Metric -> Resistor_SMD:R_0402_1005Metric
- R340: renamed from C1331; value 10n -> 100k; footprint Capacitor_SMD:C_0402_1005Metric -> Resistor_SMD:R_0402_1005Metric
- R341: renamed from C1332; value 10n -> 10k; footprint Capacitor_SMD:C_0402_1005Metric -> Resistor_SMD:R_0402_1005Metric
- R410: renamed from C1033; value 10n -> 100k; footprint Capacitor_SMD:C_0402_1005Metric -> Resistor_SMD:R_0402_1005Metric
- R411: renamed from F10; value 3A hold 1812 -> 10k; footprint Fuse:Fuse_1812_4532Metric -> Resistor_SMD:R_0402_1005Metric
- R420: renamed from C1133; value 10n -> 100k; footprint Capacitor_SMD:C_0402_1005Metric -> Resistor_SMD:R_0402_1005Metric
- R421: renamed from F11; value 3A hold 1812 -> 10k; footprint Fuse:Fuse_1812_4532Metric -> Resistor_SMD:R_0402_1005Metric
- R430: renamed from C1233; value 10n -> 100k; footprint Capacitor_SMD:C_0402_1005Metric -> Resistor_SMD:R_0402_1005Metric
- R431: renamed from F12; value 3A hold 1812 -> 10k; footprint Fuse:Fuse_1812_4532Metric -> Resistor_SMD:R_0402_1005Metric
- R440: renamed from C1333; value 10n -> 100k; footprint Capacitor_SMD:C_0402_1005Metric -> Resistor_SMD:R_0402_1005Metric
- R441: renamed from F13; value 3A hold 1812 -> 10k; footprint Fuse:Fuse_1812_4532Metric -> Resistor_SMD:R_0402_1005Metric
- R500: renamed from C501; value 22u 10V -> 10k; footprint Capacitor_SMD:C_0805_2012Metric -> Resistor_SMD:R_0402_1005Metric
- R501: renamed from C5102; value 22u 10V -> 10k; footprint Capacitor_SMD:C_0805_2012Metric -> Resistor_SMD:R_0402_1005Metric
- R502: renamed from R505; value 470 -> 0R (cap DNP alt); footprint Resistor_SMD:R_0402_1005Metric -> Capacitor_SMD:C_0402_1005Metric
- R503: renamed from C502; value 1n -> 0R (cap DNP alt)
- R504: renamed from C5103; value 22u 10V -> 10k; footprint Capacitor_SMD:C_0805_2012Metric -> Resistor_SMD:R_0402_1005Metric
- R505: renamed from R500; value 10k -> 470
- R510: renamed from F14; value 2A hold 1812 -> 10k; footprint Fuse:Fuse_1812_4532Metric -> Resistor_SMD:R_0402_1005Metric
- R511: renamed from Q31; value P-FET -30V 6A DFN3x3 -> 1k; footprint Package_DFN_QFN:DFN-8-1EP_3x3mm_P0.65mm_EP1.5x2.25mm -> Resistor_SMD:R_0402_1005Metric
- R520: renamed from F15; value 2A hold 1812 -> 10k; footprint Fuse:Fuse_1812_4532Metric -> Resistor_SMD:R_0402_1005Metric
- R521: renamed from Q32; value P-FET -30V 6A DFN3x3 -> 1k; footprint Package_DFN_QFN:DFN-8-1EP_3x3mm_P0.65mm_EP1.5x2.25mm -> Resistor_SMD:R_0402_1005Metric
- R530: renamed from F16; value 2A hold 1812 -> 10k; footprint Fuse:Fuse_1812_4532Metric -> Resistor_SMD:R_0402_1005Metric
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- renumbered C110 to C141, C111 to C151, C112 to C152, C113 to C161, C120 to C162, C20 to C21, C2000 to C2101, C2003 to C2103, C2004 to C2104, C2005 to C2105, C2001 to C2200, C2103 to C2202, C2104 to C2203, C210 to C241, C211 to C251, C212 to C252, C213 to C261, C220 to C262, D10 to D11, D11 to D12, D12 to D13, J10 to J11, J11 to J12, J12 to J13, U10 to U11, U11 to U12, U12 to U13
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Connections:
- BT1 pad 1: GND -> VBAT
- C1 pad 1: M2_PERp0 -> 5V_SYS
- C1 pad 2: PCIE_RX_P -> GND
- C100 pad 1: +1V2 -> U1_XTALI
- C1000 pad 1: U10_LXI -> U10_XI
- C1000 pad 2: U10_VDD_CORE -> GND
- C1001 pad 1: U10_XI -> U10_XO
- C1002 pad 1: U2_DN1_TXDP -> U10_RST
- C1002 pad 2: BAY3_USB3_RX_P -> GND
- C1003 pad 1: +1V2 -> U10_VDD_CORE
- C1004 pad 1: U2_UP_TXDP -> 5V_SYS
- C1004 pad 2: USB3_1_RX_P -> GND
- C1005 pad 1: U2_UP_TXDM -> U10_VCCO
- C1005 pad 2: USB3_1_RX_N -> GND
- C1007 pad 1: 5V_SYS -> U10_VDD_CORE
- C1009 pad 1: U10_RST -> U10_VCCO
- C101 pad 1: U1_RBIAS -> U1_XTALO
- C1010 pad 1: U10_REXT -> U10_VCCO
- C1011 pad 2: U10_RST -> GND
- C1020 pad 1: U10_VCCO -> U10_UTXP
- C1020 pad 2: BAY1_LED_A -> BAY1_USB3_TX_P
- C1021 pad 1: U10_XI -> U10_UTXN
- C1021 pad 2: GND -> BAY1_USB3_TX_N
- C1030 pad 1: U10_XO -> U10_STXP
- C1030 pad 2: GND -> BAY1_SATA_A_P
- C1031 pad 1: U10_VDD_CORE -> U10_STXN
- C1031 pad 2: GND -> BAY1_SATA_A_N
- C1032 pad 1: U10_VDD_CORE -> BAY1_SATA_B_P
- C1032 pad 2: GND -> U10_SRXP
- C1033 pad 1: U10_VCCO -> BAY1_SATA_B_N
- C1033 pad 2: GND -> U10_SRXN
- C110 pad 2: U1_VBUS_DET -> GND
- C1100 pad 1: U11_LXI -> U11_XI
- C1100 pad 2: U11_VDD_CORE -> GND
- C1101 pad 1: U11_XI -> U11_XO
- C1102 pad 1: BAY_EN1 -> U11_RST
- C1103 pad 1: Q31_G -> U11_VDD_CORE
- C1103 pad 2: Q51_D -> GND
- C1104 pad 1: 5V_HDD -> 5V_SYS
- C1104 pad 2: Q41_G -> GND
- C1105 pad 1: Q41_G -> U11_VCCO
- C1105 pad 2: Q61_D -> GND
- C1107 pad 1: 5V_SYS -> U11_VDD_CORE
- C1109 pad 1: U11_RST -> U11_VCCO
- C111 pad 2: U1_RESET_N -> GND
- C1110 pad 1: U11_REXT -> U11_VCCO
- C1111 pad 2: U11_RST -> GND
- C112 pad 1: U1_CFG_NON_REM -> +3V3
- C1120 pad 1: U11_VCCO -> U11_UTXP
- C1120 pad 2: BAY2_LED_A -> BAY2_USB3_TX_P
- C1121 pad 1: U11_XI -> U11_UTXN
- C1121 pad 2: GND -> BAY2_USB3_TX_N
- C113 pad 2: U1_PRT_DIS_P3 -> GND
- C1130 pad 1: U11_XO -> U11_STXP
- C1130 pad 2: GND -> BAY2_SATA_A_P
- C1131 pad 1: U11_VDD_CORE -> U11_STXN
- C1131 pad 2: GND -> BAY2_SATA_A_N
- C1132 pad 1: U11_VDD_CORE -> BAY2_SATA_B_P
- C1132 pad 2: GND -> U11_SRXP
- C1133 pad 1: U11_VCCO -> BAY2_SATA_B_N
- C1133 pad 2: GND -> U11_SRXN
- C120 pad 1: +3V3 -> +1V2
- C120 pad 2: U1_PRT_DIS_P4 -> GND
- C1200 pad 1: U12_LXI -> U12_XI
- C1200 pad 2: U12_VDD_CORE -> GND
- C1201 pad 1: U12_XI -> U12_XO
- C1202 pad 1: BAY_EN2 -> U12_RST
- C1203 pad 1: Q32_G -> U12_VDD_CORE
- C1203 pad 2: Q52_D -> GND
- C1204 pad 1: 5V_HDD -> 5V_SYS
- C1204 pad 2: Q42_G -> GND
- C1205 pad 1: Q42_G -> U12_VCCO
- C1205 pad 2: Q62_D -> GND
- C1207 pad 1: 5V_SYS -> U12_VDD_CORE
- C1209 pad 1: U12_RST -> U12_VCCO
- C121 pad 1: +3V3 -> +1V2
- C121 pad 2: U1_PRT_DIS_M3 -> GND
- C1210 pad 1: U12_REXT -> U12_VCCO
- C1211 pad 2: U12_RST -> GND
- C122 pad 1: +3V3 -> +1V2
- C122 pad 2: U1_PRT_DIS_M4 -> GND
- C1220 pad 1: U12_VCCO -> U12_UTXP
- C1220 pad 2: BAY3_LED_A -> BAY3_USB3_TX_P
- C1221 pad 1: U12_XI -> U12_UTXN
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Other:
- board size 150 x 98 mm -> 136 x 100 mm
- board text added: "brain-drain carrier v2 136x100 rear edge = top"
- board text removed: "brain-drain carrier v1 150x98 rear edge = top"
